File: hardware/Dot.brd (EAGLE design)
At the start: 23.3 x 31.5 mm, 25 parts, among them IC1 CAT24M010TS, U1 ATMEGA328P-MU-QFN32, U2 TMP102

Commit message: v0.5
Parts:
- removed SJ3: (no value), SparkFun:SJ_3
- removed U$3: MPU-9250, invensense:LEAD-QFN24
- added C4, C8: 0.1uF, resistor:C0603
- added C5, C7: (no value), resistor:C0603
- added C6: 1uF, resistor:C0603
- added IC2: SI1145, silabs:QFN-10
- added L1: 3.3µH/±20%/450mA, SparkFun-Coils:0805
- added SJ5: (no value), SparkFun:SJ_3
- added U3: ISL29125, SparkFun-Sensors:ODFN-6
- added U4: 9DoF IMU, SparkFun-Sensors:QFN24-3X3
- R3: value 1kΩ -> 10kΩ
- moved C1 42.8 mm to (31.0, 40.2), turned to 180 degrees
- moved C2 36.9 mm to (30.0, 29.1), turned to 0 degrees
- moved C3 31.6 mm to (30.0, 31.2)
- moved LOGO1 27.4 mm to (35.7, 25.2), flipped to the bottom
- moved U2 25.9 mm to (29.7, 26.4)
- moved X1 22.0 mm to (35.9, 39.9)
- moved SJ2 21.9 mm to (36.2, 39.4)
- moved IC1 21.5 mm to (16.6, 31.2)
- moved JP3 21.5 mm to (24.0, 46.2)
- moved LED1 21.5 mm to (15.0, 39.9)
- moved R1 21.5 mm to (15.0, 39.9)
- moved R3 21.5 mm to (30.4, 17.5)
- moved R7 21.5 mm to (30.4, 36.3)
- moved SJ4 21.5 mm to (27.1, 18.3)
- moved U$1 21.5 mm to (26.1, 31.6)
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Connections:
- removed net ANT_2: ANT1.1, SJ2.2
- removed net N$8: C2.1, U$3.10
- new net ANT: ANT1.1, C5.1, L1.1, SJ2.2
- new net INT_RGB: U1.7, U3.5
- new net INT_UV: IC2.4, U1.8
- new net N$11: C8.1, U4.10
- new net N$14: SJ5.2, U4.9
- net +3V3: now also C2.1, C4.1, C6.1, IC2.3, JP2.3, SJ5.3, U3.1, U4.13; no longer JP2.2, SJ3.3, U$3.13
- net GND: now also C4.2, C5.2, C6.2, C7.2, C8.2, IC2.8, JP2.4, SJ5.1, U3.3, U4.18, U4.20; no longer JP2.1, SJ3.1, U$3.18
- net MOVE_INT: now also U4.12; no longer U$3.12
- net N$9: now also C7.1, L1.2; no longer SJ3.2, U$3.9
- net SCL: now also IC2.2, JP2.2, U3.6, U4.23; no longer JP2.4, U$3.23
- net SDA: now also IC2.1, JP2.1, U3.4, U4.24; no longer JP2.3, U$3.24
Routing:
- net SDA: track 45.5 -> 84.6 mm, vias 3 -> 7
- net +3V3: track 86.7 -> 119.4 mm, vias 2 -> 3
- net INT_UV: track 0.00 -> 26.1 mm, vias 0 -> 2
- net SCL: track 54.9 -> 74.1 mm, vias 2 -> 5
- net INT_RGB: track 0.00 -> 13.8 mm, vias 0 -> 2
- net RIRQ: track 26.1 -> 14.5 mm, vias 1 -> 2
- net N$14: track 0.00 -> 9.39 mm, vias 0 -> 1
- net GND: track 48.7 -> 57.0 mm, vias 25 -> 63
- net TXD: track 23.9 -> 15.8 mm
- net N$9: track 6.97 -> 0.00 mm, vias 1 -> 0
- net N$12: track 0.00 -> 6.95 mm
- net SCK: track 21.4 -> 26.3 mm
- net PUSH: track 19.0 -> 14.2 mm, vias 1 -> 2
- net ANT_1: track 3.94 -> 0.00 mm
- net RSCK: track 14.6 -> 10.6 mm, vias 2 -> 1
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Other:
- board size 23.3 x 31.5 mm -> 23.9 x 31.5 mm
- board text added: "Dot v0.5"
- board text added: "HexID"
- board text removed: "01.2017"
- board text removed: "Mihai Galos Dot v0.3"

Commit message: v1.3
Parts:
- removed JP3: (no value), pinhead:1X08
- removed R1: 150Ω, resistor:R0603
- added JP1: (no value), pinhead:1X10
- added R5: 130Ω, resistor:R0603
- added R6, R8: 30Ω, resistor:R0603
- added SPK1: SMT-0540-S-R, adafruit:SMT-0540-S-R
- added U$3: AT45DB641E, AT45DB641E:UDFN-8
- added U$4: LDCL015, LDCL015:SOT23-5
- added U5: BMP18, Seeed-OPL-sensor:LGA7-1.5-3.8X3.6MM
- LED1: value (none) -> GM1WA55311A; device SparkFun:LED-0603 -> led:GM1WA55311A
- moved IC2 26.7 mm to (17.2, 27.0)
- moved C6 26.4 mm to (17.6, 27.1)
- moved LOGO1 25.9 mm to (21.7, 3.49), flipped to the top
- moved R4 22.9 mm to (2.58, 24.0)
- moved U3 21.2 mm to (17.4, 4.37)
- moved C8 20.9 mm to (6.62, 6.09), turned to 270 degrees
- moved C4 20.8 mm to (17.5, 4.39)
- moved C2 20.3 mm to (17.0, 13.4)
- moved R3 20.3 mm to (17.4, 1.83)
- moved R7 20.3 mm to (17.4, 20.6)
- moved C1 20.3 mm to (18.1, 24.5)
- moved C3 20.3 mm to (17.0, 15.5)
- moved JP2 20.3 mm to (5.96, 2.55)
- moved SJ4 20.3 mm to (14.1, 2.58)
- moved SJ5 20.3 mm to (12.1, 2.59)
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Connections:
- removed net ADC1: JP3.2, R4.1, U1.24
- removed net N$7: LED1.A, R1.2
- new net ADC: JP1.2, R4.1, U1.19
- new net BUZZER: SPK1.+, U1.23
- new net FLASH_CS: U$3.4, U1.24
- new net N$1: LED1.3, R8.1
- new net N$15: LED1.1, R5.1
- new net RXD: JP1.4, R5.2, U1.30
- new net VIN: JP1.6, U$4.1, U$4.3
- net +3V3: now also LED1.4, U$3.3, U$3.6, U$4.5, U1.18, U4.1, U4.8, U5.2, U5.3; no longer JP3.4
- net GND: now also JP1.5, SPK1.-, SW1.2, U$3.7, U$3.THERM, U$4.2, U4.11, U5.7; no longer JP3.3, LED1.C, R7.8
- net LED: now also R8.2; no longer R1.1
- net LIGHT_SENSE: now also U1.22; no longer U1.23
- net MISO: now also JP1.9, U$3.8; no longer JP3.7
- net MOSI: now also JP1.10, U$3.1; no longer JP3.8
- net MOVE_INT: now also U1.25; no longer U1.30
- net N$4: now also LED1.2, R6.1; no longer R7.1, SW1.2
- net PUSH: now also JP1.1, U1.1; no longer U1.32
- net RIRQ: now also U1.32; no longer U1.26
- net RSEL: now also U1.26; no longer U1.1
- net RST: now also JP1.7; no longer JP3.5
- net SCK: now also JP1.8, U$3.2; no longer JP3.6
- net SCL: now also U5.5
- net SDA: now also U5.6
- net TXD: now also JP1.3, R6.2; no longer JP3.1
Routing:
- net GND: track 57.0 -> 134.5 mm, vias 63 -> 57
- net MOSI: track 23.0 -> 49.7 mm, vias 1 -> 2
- net ADC: track 0.00 -> 21.3 mm, vias 0 -> 3
- net N$4: track 23.2 -> 2.39 mm
- net MISO: track 28.2 -> 48.9 mm, vias 1 -> 5
- net PUSH: track 14.2 -> 34.0 mm
- net RXD: track 0.00 -> 19.1 mm, vias 0 -> 1
- net ADC1: track 18.2 -> 0.00 mm
- net SCK: track 26.3 -> 41.4 mm, vias 1 -> 2
- net BUZZER: track 0.00 -> 14.8 mm, vias 0 -> 3
- net FLASH_CS: track 0.00 -> 13.3 mm
- net +3V3: track 119.4 -> 128.9 mm, vias 3 -> 7
- net INT_UV: track 26.1 -> 17.1 mm
- net SCL: track 74.1 -> 82.7 mm
- net RSEL: track 14.2 -> 6.23 mm
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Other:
- board size 23.9 x 31.5 mm -> 25.4 x 31.5 mm
- board text added: "05.2017"
- board text added: "3V3"
- board text added: "ADC"
- board text added: "Dot v1.3"
- board text added: "EEP"
- board text added: "GND"
- board text added: "INT1"
- board text added: "MISO"
- board text added: "MOSI"
- board text added: "Mihai Galos"
- board text added: "RxD"
- board text added: "SCK"
- board text added: "SCL"
- board text added: "SDA"
- board text added: "TxD"
- board text added: "VCC"
- board text removed: "Dot v0.5"
- board text removed: "I2C EEPROM"
- board text removed: "Light"

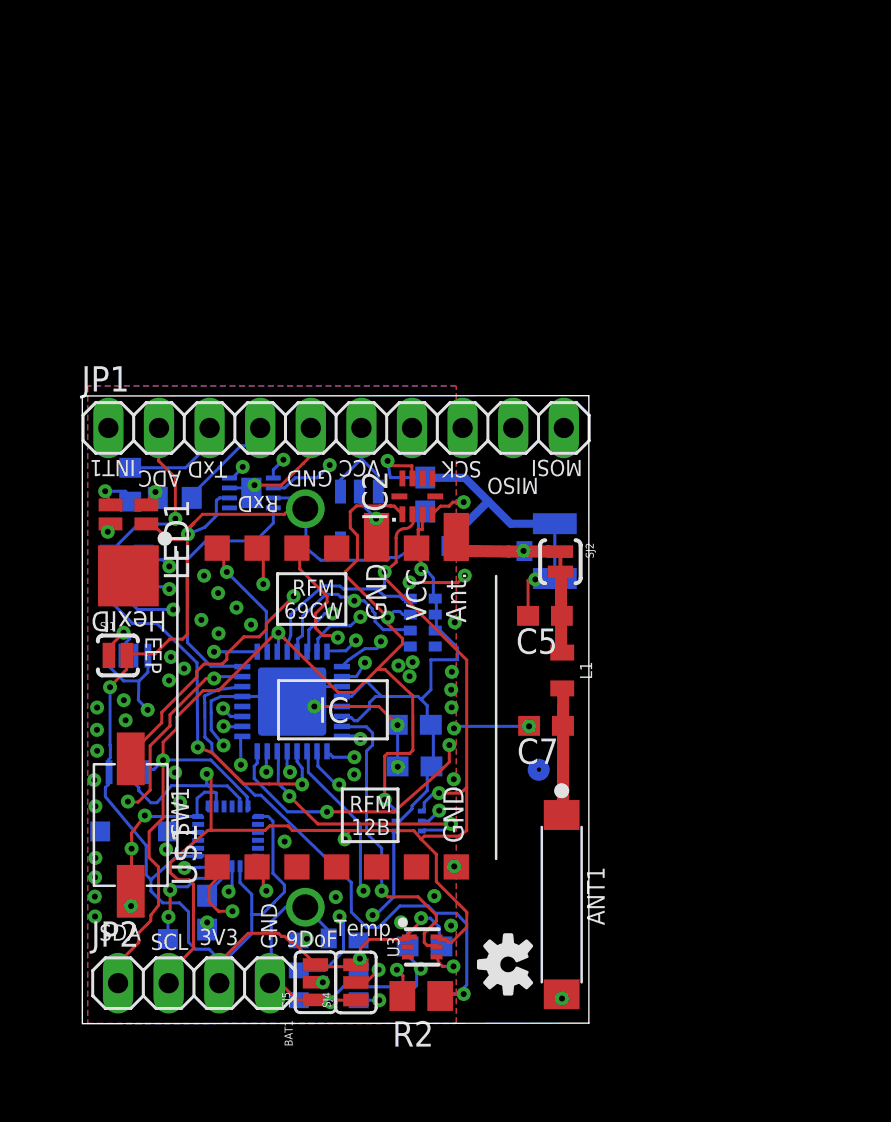
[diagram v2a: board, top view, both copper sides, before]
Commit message: * Corrected RGB Led layout * Added 100uF Cap. Should soften discharges up to 30mA for 1ms. * Cap recharges in 175ms.
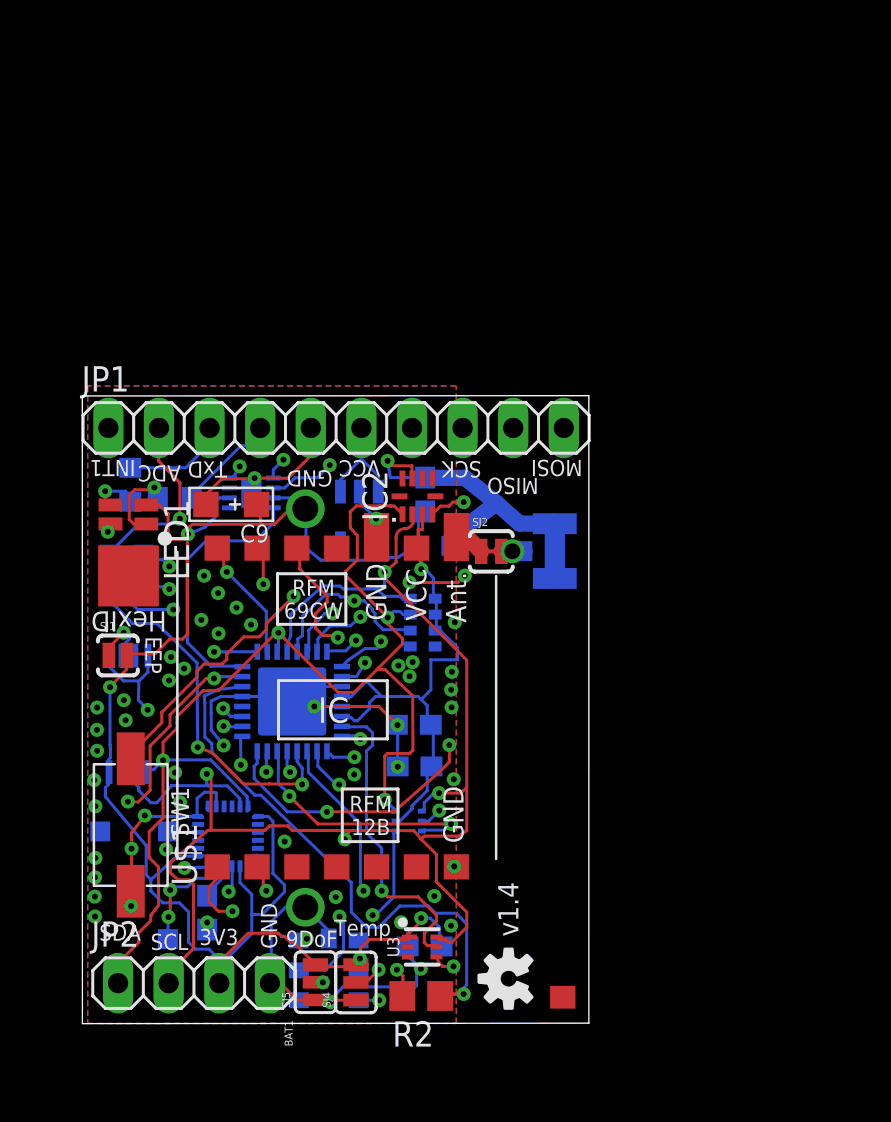
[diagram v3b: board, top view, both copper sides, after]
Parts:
- removed ANT1: AN9520, Seeed-OPL-Antenna:ANT2-SMD-9.5X2X1.2MM
- removed C5, C7: (no value), resistor:C0603
- removed L1: 3.3µH/±20%/450mA, SparkFun-Coils:0805
- added C9: 100uf, Seeed-OPL-Capacitor:AVX-A
- moved SJ2 3.51 mm to (20.9, 24.2), turned to 0 degrees
- moved LOGO1 0.72 mm to (21.8, 2.77)
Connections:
- removed net ANT: ANT1.1, C5.1, L1.1, SJ2.2
- removed net ANT_1: SJ2.1, U$1.ANT, X1.3
- removed net N$9: C7.1, L1.2
- new net N$3: SJ2.1, U$1.ANT
- new net N$7: SJ2.2, X1.3
- net +3V3: now also C9.+
- net GND: now also C9.-; no longer C5.2, C7.2
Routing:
- net N$12: track 6.45 -> 0.00 mm
- net GND: track 134.5 -> 130.4 mm, vias 57 -> 54
- net N$8: track 3.84 -> 0.00 mm
- net N$15: track 1.30 -> 4.28 mm
- net N$5: track 2.47 -> 0.00 mm
- net +3V3: track 128.9 -> 131.1 mm
- net N$7: track 0.00 -> 1.16 mm, vias 0 -> 1
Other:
- board text added: "v1.4"
- board text removed: "05.2017"
- board text removed: "Dot v1.3"
- board text removed: "Mihai Galos"
- board text removed: "RxD"

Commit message: Rearranging files
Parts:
- removed C6: 1uF, resistor:C0603
- removed C9: 100uf, Seeed-OPL-Capacitor:AVX-A
- removed SJ1: SOLDERJUMPERNO, SparkFun:SJ_2S-NO
- added C10: 1500uF 4V, adafruit:CT7343
- added C5: 100uf, Seeed-OPL-Capacitor:AVX-A
- added C7: 1uF, resistor:C0603
- added JP3, JP4: JUMPER-SMT_2_NO_NO-SILK, SparkFun-Jumpers:SMT-JUMPER_2_NO_NO-SILK
- added R1, R9: (no value), resistor:R0603
- added SJ3: SOLDERJUMPERNC2, SparkFun:SJ_2S-NOTRACE
- added U$2: DIODE-ZENER-BZT52, SparkFun:SOD-323
- added Y1: (no value), SparkFun-Clocks:RESONATOR-SMD-3.2X1.3
- R5: value 130Ω -> 67Ω
- R6, R8: value 30Ω -> 67Ω
- U$3: value AT45DB641E -> AT25SF081; device AT45DB641E:UDFN-8 -> AT25SF081:DFN-2X3
- moved R8 1.57 mm to (2.60, 24.0), turned to 180 degrees
- moved R4 1.48 mm to (2.60, 22.5)
- moved C2 0.97 mm to (16.3, 12.8)
- moved U$3 0.96 mm to (8.22, 26.4), turned to 270 degrees
- moved C3 0.89 mm to (17.8, 15.8), turned to 90 degrees
- moved LOGO1 0.45 mm to (21.3, 2.63)
- moved LED1 0.07 mm to (2.68, 26.0)
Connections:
- removed net INT_RGB: U1.7, U3.5
- removed net INT_UV: IC2.4, U1.8
- removed net N$2: IC1.A1, SJ1.1
- removed net TEMP_ALERT: U1.14, U2.3
- new net INT_MULTIPLE: IC2.4, R7.1, U1.14, U2.3, U3.5
- new net N$5: C7.2, JP1.7, JP3.2
- new net N$6: U1.7, Y1.3
- new net N$8: U1.8, Y1.1
- new net VIN_PIN: JP1.6, JP4.1, R9.2
- net +3V3: now also C10.+, C5.+, R7.8, SJ3.2, U$2.1, U$3.7, U$3.8; no longer C6.1, C9.+, SJ1.2, U$3.6
- net FLASH_CS: now also U$3.1; no longer U$3.4
- net GND: now also C10.-, C5.-, R1.1, U$2.2, U$3.4, Y1.2; no longer C6.2, C9.-, U$3.7, U$3.THERM
- net LED: now also R5.2; no longer R8.2
- net MISO: now also U$3.2; no longer U$3.8
- net MOSI: now also U$3.5; no longer U$3.1
- net RST: now also C7.1, JP3.1; no longer JP1.7
- net RXD: now also R6.2; no longer R5.2
- net SCK: now also U$3.6; no longer U$3.2
- net TXD: now also R8.2; no longer R6.2
- net VIN: now also JP4.2, R1.2, R9.1, SJ3.1; no longer JP1.6
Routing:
- net INT_MULTIPLE: track 0.00 -> 48.9 mm, vias 0 -> 6
- net INT_UV: track 17.1 -> 0.00 mm, vias 2 -> 0
- net INT_RGB: track 15.7 -> 0.00 mm, vias 1 -> 0
- net +3V3: track 131.1 -> 144.0 mm, vias 7 -> 11
- net TEMP_ALERT: track 12.8 -> 0.00 mm, vias 2 -> 0
- net SCK: track 41.4 -> 49.9 mm
- net MOSI: track 49.7 -> 55.9 mm
- net TXD: track 22.0 -> 28.0 mm, vias 1 -> 3
- net LED: track 19.0 -> 24.5 mm
- net RSDO: track 16.3 -> 11.3 mm
- net N$5: track 0.00 -> 4.66 mm
- net N$1: track 6.27 -> 2.00 mm, vias 2 -> 1
- net SDA: track 80.1 -> 84.4 mm
- net RST: track 19.3 -> 16.4 mm, vias 1 -> 2
- net N$2: track 2.90 -> 0.00 mm, vias 1 -> 0
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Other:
- board text added: "12.2017"
- board text added: "868Mhz"
- board text added: "915Mhz"
- board text added: "9D"
- board text added: "Mihai Galos"
- board text added: "RxD"
- board text added: "v1.6.1"
- board text removed: "9DoF"
- board text removed: "EEP"
- board text removed: "VCC"
- board text removed: "v1.4"

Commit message: Removing superfluous extra MOSI.
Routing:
- net MOSI: track 55.9 -> 41.2 mm
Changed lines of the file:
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@@
 <grid distance="0.01" unitdist="mm" unit="mm" style="lines" multiple="1" display="yes" altdistance="0.0025" altunitdist="inch" altunit="inch"/>
 <layers>
-<layer number="1" name="Top" color="4" fill="1" visible="yes" active="yes"/>
-<layer number="2" name="Route2" color="1" fill="3" visible="yes" active="yes"/>
+<layer number="1" name="Top" color="4" fill="1" visible="no" active="yes"/>
+<layer number="2" name="Route2" color="1" fill="3" visible="no" active="yes"/>
 <layer number="3" name="Route3" color="4" fill="3" visible="no" active="no"/>
 <layer number="14" name="Route14" color="1" fill="6" visible="no" active="no"/>
-<layer number="15" name="Route15" color="4" fill="6" visible="yes" active="yes"/>
-<layer number="16" name="Bottom" color="1" fill="1" visible="yes" active="yes"/>
-<layer number="17" name="Pads" color="2" fill="1" visible="yes" active="yes"/>
-<layer number="18" name="Vias" color="2" fill="1" visible="yes" active="yes"/>
+<layer number="15" name="Route15" color="4" fill="6" visible="no" active="yes"/>
+<layer number="16" name="Bottom" color="1" fill="1" visible="no" active="yes"/>
+<layer number="17" name="Pads" color="2" fill="1" visible="no" active="yes"/>
+<layer number="18" name="Vias" color="2" fill="1" visible="no" active="yes"/>
 <layer number="19" name="Unrouted" color="6" fill="1" visible="yes" active="yes"/>
 <layer number="20" name="Dimension" color="15" fill="1" visible="yes" active="yes"/>
-<layer number="21" name="tPlace" color="7" fill="1" visible="yes" active="yes"/>
+<layer number="21" name="tPlace" color="7" fill="1" visible="no" active="yes"/>
 <layer number="22" name="bPlace" color="7" fill="1" visible="no" active="yes"/>
 <layer number="23" name="tOrigins" color="15" fill="1" visible="no" active="yes"/>
-<layer number="24" name="bOrigins" color="15" fill="1" visible="yes" active="yes"/>
+<layer number="24" name="bOrigins" color="15" fill="1" visible="no" active="yes"/>
 <layer number="25" name="tNames" color="7" fill="1" visible="no" active="yes"/>
 <layer number="26" name="bNames" color="7" fill="1" visible="no" active="yes"/>
@@
 <wire x1="24.37485625" y1="30.501590625" x2="24.524715625" y2="30.41523125" width="0.1524" layer="2"/>
 <via x="9.59205625" y="13.153390625" extent="1-16" drill="0.3"/>
-<wire x1="10.44295625" y1="30.900371875" x2="10.97635625" y2="31.436309375" width="0.1524" layer="15"/>
-<wire x1="10.97635625" y1="31.436309375" x2="23.432515625" y2="31.436309375" width="0.1524" layer="15"/>
-<wire x1="23.432515625" y1="31.436309375" x2="24.524715625" y2="30.41523125" width="0.1524" layer="15"/>
 <contactref element="U$3" pad="5"/>
 <wire x1="8.97" y1="25.095" x2="8.96" y2="25.095" width="0.1524" layer="16"/>
